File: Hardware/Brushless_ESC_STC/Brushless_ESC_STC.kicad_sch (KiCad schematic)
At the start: 71 parts, among them J1 Conn_01x04_Male, J2 Conn_01x01_Male, J3 Conn_01x01_Male, J4 Conn_01x01_Male, J5 Conn_01x01_Male, J6 Conn_01x01_Male, J7 Conn_01x01_Male, J8 Conn_01x01_Male, J9 Conn_01x01_Male, Q1 S8050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

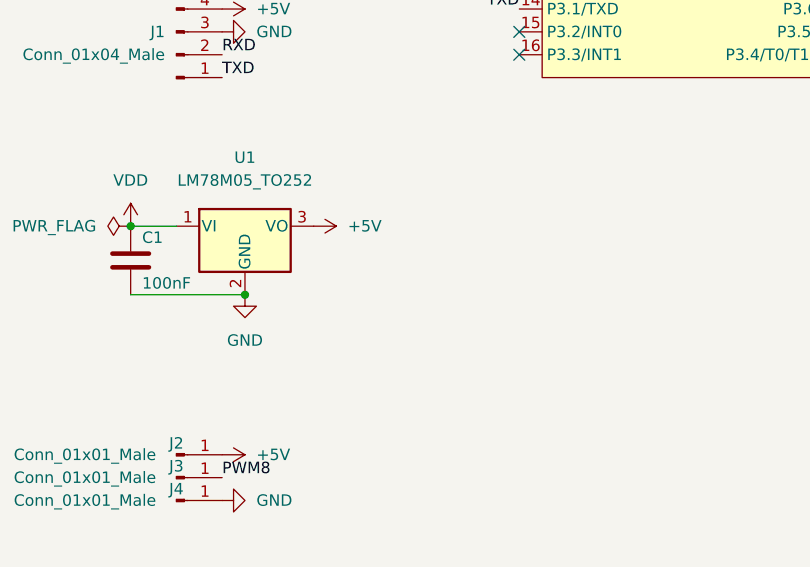
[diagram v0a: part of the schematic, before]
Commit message: 添加STC8H1K28的QFN封装与FD6288的无刷电调原理图及布局
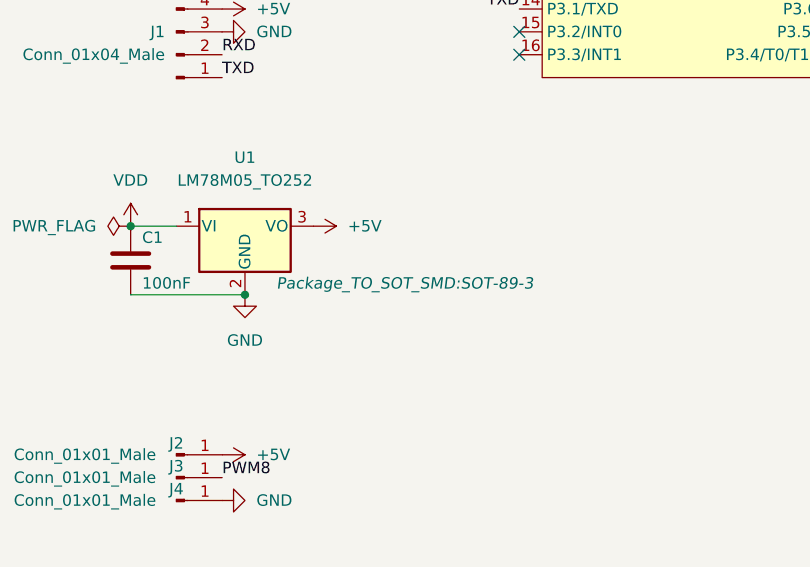
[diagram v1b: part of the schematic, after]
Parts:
- U1: footprint Package_TO_SOT_SMD:TO-252-2 -> Package_TO_SOT_SMD:SOT-89-3
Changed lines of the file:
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@@
   )
   (symbol (lib_id "Regulator_Linear:LM78M05_TO252") (at 44.45 114.3 0) (unit 1)
-    (in_bom yes) (on_board yes) (fields_autoplaced)
+    (in_bom yes) (on_board yes)
     (property "Reference" "U1" (id 0) (at 44.45 106.68 0))
     (property "Value" "LM78M05_TO252" (id 1) (at 44.45 109.22 0))
-    (property "Footprint" "Package_TO_SOT_SMD:TO-252-2" (id 2) (at 44.45 108.585 0)
-      (effects (font (size 1.27 1.27) italic) hide)
+    (property "Footprint" "Package_TO_SOT_SMD:SOT-89-3" (id 2) (at 62.23 120.65 0)
+      (effects (font (size 1.27 1.27) italic))
     )
     (property "Datasheet" "https://www.onsemi.com/pub/Collateral/MC78M00-D.PDF" (id 3) (at 44.45 115.57 0)
@@
     )
     (path "/aa9085ff-e595-4ff7-981b-9067cf2a81b4"
-      (reference "U1") (unit 1) (value "LM78M05_TO252") (footprint "Package_TO_SOT_SMD:TO-252-2")
+      (reference "U1") (unit 1) (value "LM78M05_TO252") (footprint "Package_TO_SOT_SMD:SOT-89-3")
     )
     (path "/29023932-9eaf-407f-9d5c-ad492a2312e5"
